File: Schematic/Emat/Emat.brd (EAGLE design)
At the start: 100 x 80 mm, 38 parts, among them J1 PIN1-2, J10 PIN1-2, J11 PIN1-2, J2 PIN1-2, J3 PIN1-2, J4 PIN1-2, J5 PIN1-2, J6 PIN1-2, J7 PIN1-2, J8 PIN1-2, J9 PIN1-2, Q2 STP13NM60NTO220BVH, U1 UCC27324D, X1 SMA-J502-ND

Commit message: Further work on schematic.
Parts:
- removed C8: 220p 630v, rcl:C1206K
- added C9: 220pF 1000V, rcl:C075-042X103
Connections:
- net N$13: now also C9.2; no longer C8.2
- net N$16: now also C9.1; no longer C8.1
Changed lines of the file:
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@@
 <element name="C6" library="rcl" package="C0805" value="1uF 16V" x="57.15" y="68.58" rot="R90"/>
 <element name="C7" library="rcl" package="C0805" value="1uF 16V" x="52.07" y="68.58" rot="R90"/>
-<element name="C8" library="rcl" package="C1206K" value="220p 630v" x="82.55" y="57.15" rot="R180"/>
 <element name="D1" library="diode" package="DO41-10" value="MUR160" x="88.9" y="43.18" rot="R180"/>
 <element name="D2" library="diode" package="DO41-10" value="MUR160" x="88.9" y="36.83" rot="R180"/>
@@
 <attribute name="OC_NEWARK" value="16H2318" x="-63.5" y="6.35" size="1.778" layer="27" display="off"/>
 </element>
+<element name="C9" library="rcl" package="C075-042X103" value="220pF 1000V" x="-63.5" y="-5.08"/>
 </elements>
 <signals>
@@
 </signal>
 <signal name="N$13">
-<contactref element="C8" pad="2"/>
 <contactref element="R10" pad="1"/>
-<wire x1="81.05" y1="57.15" x2="81.432" y2="53.34" width="0" layer="19" extent="1-1"/>
+<contactref element="C9" pad="2"/>
+<wire x1="-59.69" y1="-5.08" x2="81.432" y2="53.34" width="0" layer="19" extent="1-1"/>
 </signal>
 <signal name="N$14">
@@
 </signal>
 <signal name="N$16">
-<contactref element="C8" pad="1"/>
 <contactref element="C2" pad="2"/>
 <contactref element="C3" pad="2"/>
@@
 <contactref element="D2" pad="C"/>
 <contactref element="D1" pad="C"/>
-<wire x1="94.24" y1="55.88" x2="95.25" y2="68.58" width="0" layer="19" extent="1-1"/>
+<contactref element="C9" pad="1"/>
+<wire x1="95.25" y1="68.58" x2="95.25" y2="73.66" width="0" layer="19" extent="1-1"/>
+<wire x1="95.25" y1="62.23" x2="95.25" y2="68.58" width="0" layer="19" extent="1-1"/>
+<wire x1="94.24" y1="55.88" x2="95.25" y2="62.23" width="0" layer="19" extent="1-1"/>
 <wire x1="94.24" y1="49.53" x2="94.24" y2="55.88" width="0" layer="19" extent="1-1"/>
-<wire x1="95.25" y1="62.23" x2="94.24" y2="49.53" width="0" layer="19" extent="1-1"/>
-<wire x1="84.05" y1="57.15" x2="95.25" y2="62.23" width="0" layer="19" extent="1-1"/>
 <wire x1="93.98" y1="43.18" x2="94.24" y2="49.53" width="0" layer="19" extent="1-1"/>
 <wire x1="93.98" y1="36.83" x2="93.98" y2="43.18" width="0" layer="19" extent="1-1"/>
-<wire x1="95.25" y1="73.66" x2="93.98" y2="36.83" width="0" layer="19" extent="1-1"/>
+<wire x1="-67.31" y1="-5.08" x2="93.98" y2="36.83" width="0" layer="19" extent="1-1"/>
 </signal>
 <signal name="N$15">

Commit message: 300V PCB modified, BOM added.
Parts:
- C1, C2, C3: value 4.7n -> 4.7n 1000V
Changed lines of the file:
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@@
 </autorouter>
 <elements>
-<element name="C1" library="capacitor-wima" package="C10B4" value="4.7n" x="90.17" y="73.66"/>
-<element name="C2" library="capacitor-wima" package="C10B4" value="4.7n" x="90.17" y="68.58"/>
-<element name="C3" library="capacitor-wima" package="C10B4" value="4.7n" x="90.17" y="62.23"/>
+<element name="C1" library="capacitor-wima" package="C10B4" value="4.7n 1000V" x="90.17" y="73.66"/>
+<element name="C2" library="capacitor-wima" package="C10B4" value="4.7n 1000V" x="90.17" y="68.58"/>
+<element name="C3" library="capacitor-wima" package="C10B4" value="4.7n 1000V" x="90.17" y="62.23"/>
 <element name="C4" library="capacitor-wima" package="C27.5B13" value="1uF 400V" x="17.78" y="62.23" rot="R270"/>
 <element name="C5" library="rcl" package="SANYO-OSCON_G" value="47uF 400V" x="8.89" y="69.85"/>

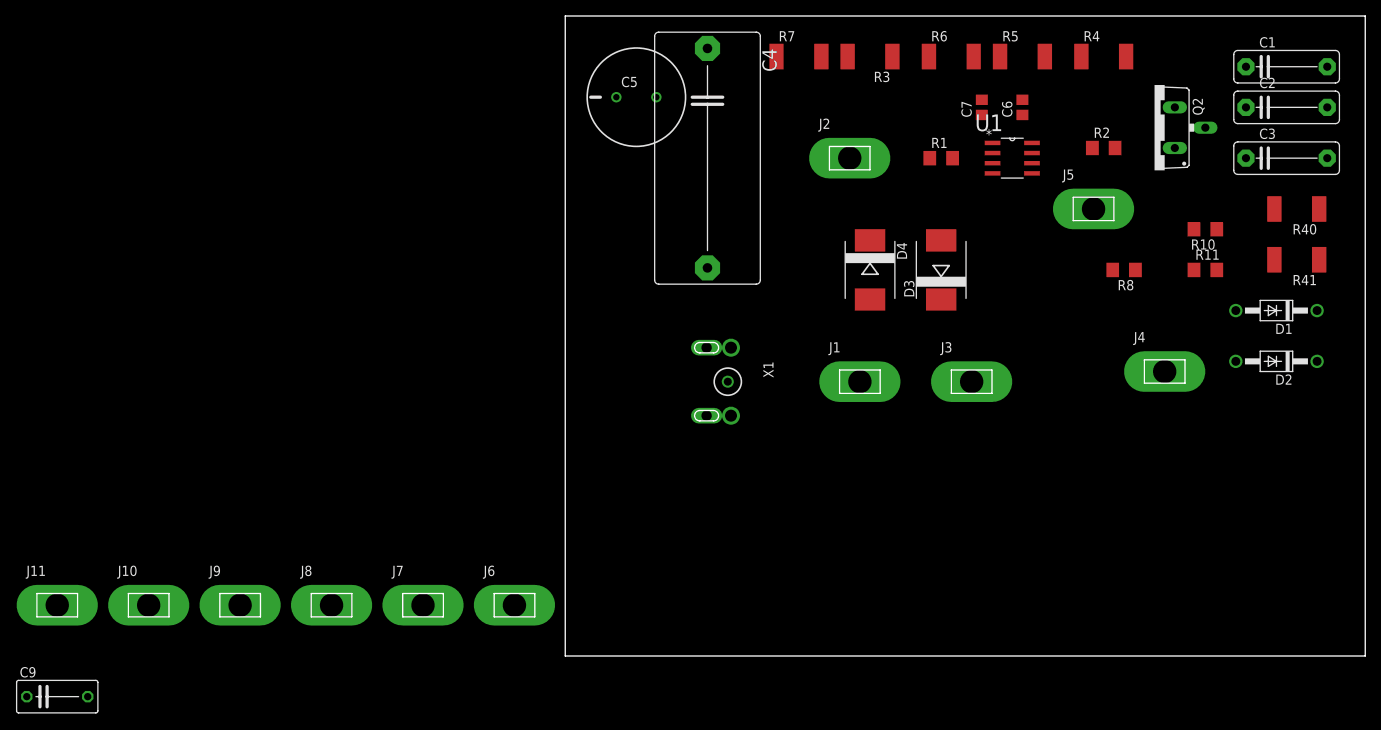
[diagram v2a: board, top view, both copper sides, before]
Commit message: Add switch tracing.
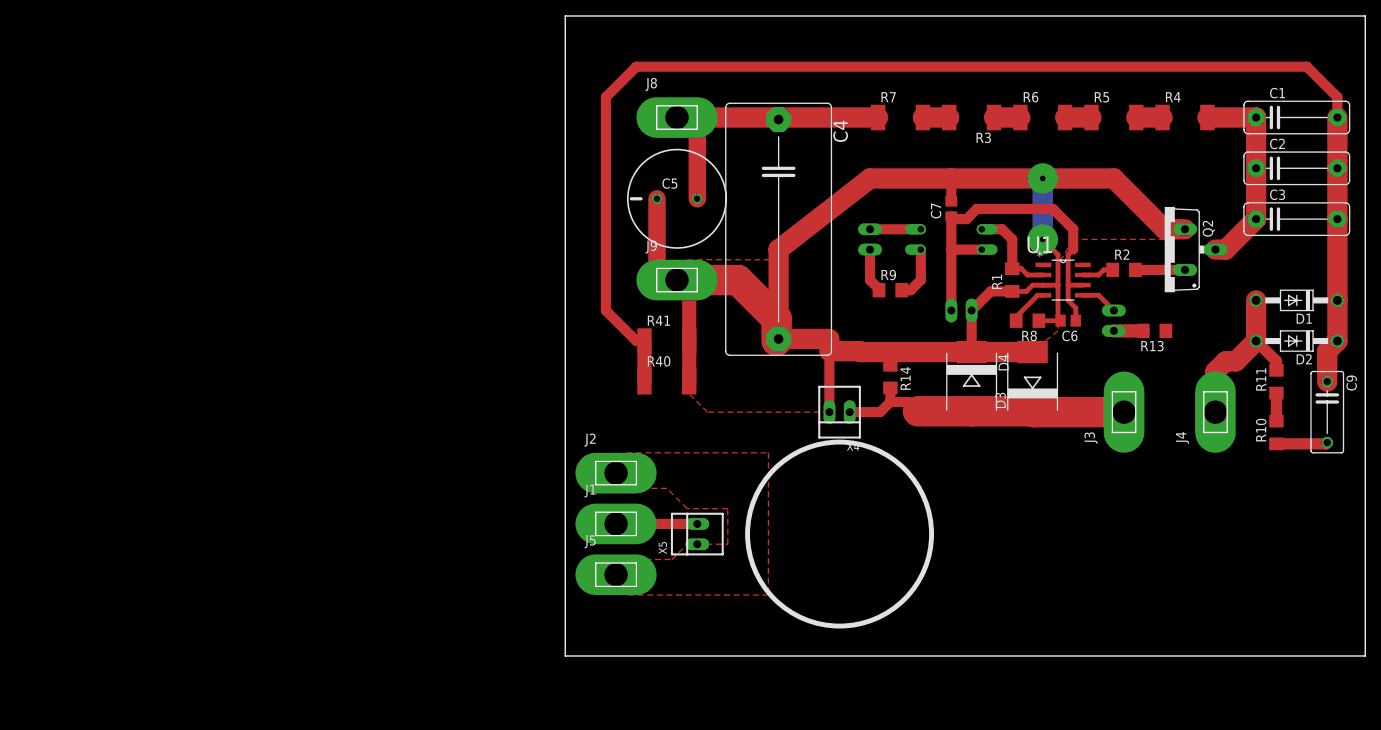
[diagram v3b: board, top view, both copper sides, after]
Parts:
- removed J10, J11, J6, J7: PIN1-2, con-faston:62221
- removed X1: SMA-J502-ND, con-coax:J502-ND
- added OK1: PC817, optocoupler:DIL04
- added R13: DNS, rcl:R1206
- added R14: 51, rcl:R1206
- added R9: 510, rcl:R1206
- added X2, X3, X4, X5, X6: 22-23-2021, con-molex:22-23-2021
- C6, C7: value 1uF 16V -> 1uF
- R1: value 51 -> 10K
- moved C9 162.7 mm to (95.2, 30.5), turned to 270 degrees
- moved R40 81.6 mm to (12.7, 34.3), turned to 0 degrees
- moved R41 79.4 mm to (12.7, 39.4), turned to 0 degrees
- moved J5 75.2 mm to (6.35, 10.2)
- moved J8 74.7 mm to (14.0, 67.3)
- moved J9 68.1 mm to (14.0, 47.0)
- moved J2 49.0 mm to (6.35, 22.9)
- moved J1 35.3 mm to (6.35, 16.5)
- moved C6 27.3 mm to (62.9, 41.9), turned to 180 degrees
- moved R10 26.9 mm to (88.9, 27.9), turned to 90 degrees
- moved J3 19.4 mm to (69.8, 30.5), turned to 90 degrees
- moved D4 18.9 mm to (50.8, 34.3)
- moved D3 18.1 mm to (58.4, 34.3)
- moved R1 17.6 mm to (55.9, 47.0), turned to 90 degrees
- moved R11 16.6 mm to (88.9, 34.3), turned to 90 degrees
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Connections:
- removed net N$5: J10.1, R1.1
- new net N$17: OK1.1, R9.2
- new net N$18: R9.1, X2.2
- new net N$19: OK1.2, X2.1
- new net N$20: D3.C, D4.A, J3.1, R14.2, X4.1
- new net N$21: R13.2, X6.2
- new net N$22: J2.1, J5.1, X5.1
- net +12V: now also OK1.4, X3.2; no longer J7.1
- net GND: now also R1.1, R14.1, X3.1, X4.2; no longer J11.1, J2.1, J6.1, X1.2, X1.3, X1.4, X1.5
- net N$1: now also OK1.3
- net N$10: now also X5.2; no longer D3.C, D4.A, J3.1, X1.1
- net N$12: now also X6.1; no longer J5.1
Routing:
- net GND: track 0.00 -> 196.2 mm, vias 0 -> 2
- net N$16: track 0.00 -> 168.8 mm
- net +12V: track 0.00 -> 46.4 mm
- net +UB: track 0.00 -> 38.1 mm
- net N$20: track 0.00 -> 37.1 mm
- net N$4: track 0.00 -> 25.4 mm
- net N$15: track 0.00 -> 21.5 mm
- net N$1: track 0.00 -> 12.2 mm
- net N$10: track 0.00 -> 10.2 mm
- net N$17: track 0.00 -> 6.72 mm
- net N$13: track 0.00 -> 6.41 mm
- net N$19: track 0.00 -> 6.35 mm
- net N$3: track 0.00 -> 6.20 mm
- net N$18: track 0.00 -> 5.54 mm
- net N$11: track 0.00 -> 5.00 mm
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- added copper zone on layer 1, net GND
- added copper zone on layer 1, net N$22
- added copper zone on layer 1, net N$5

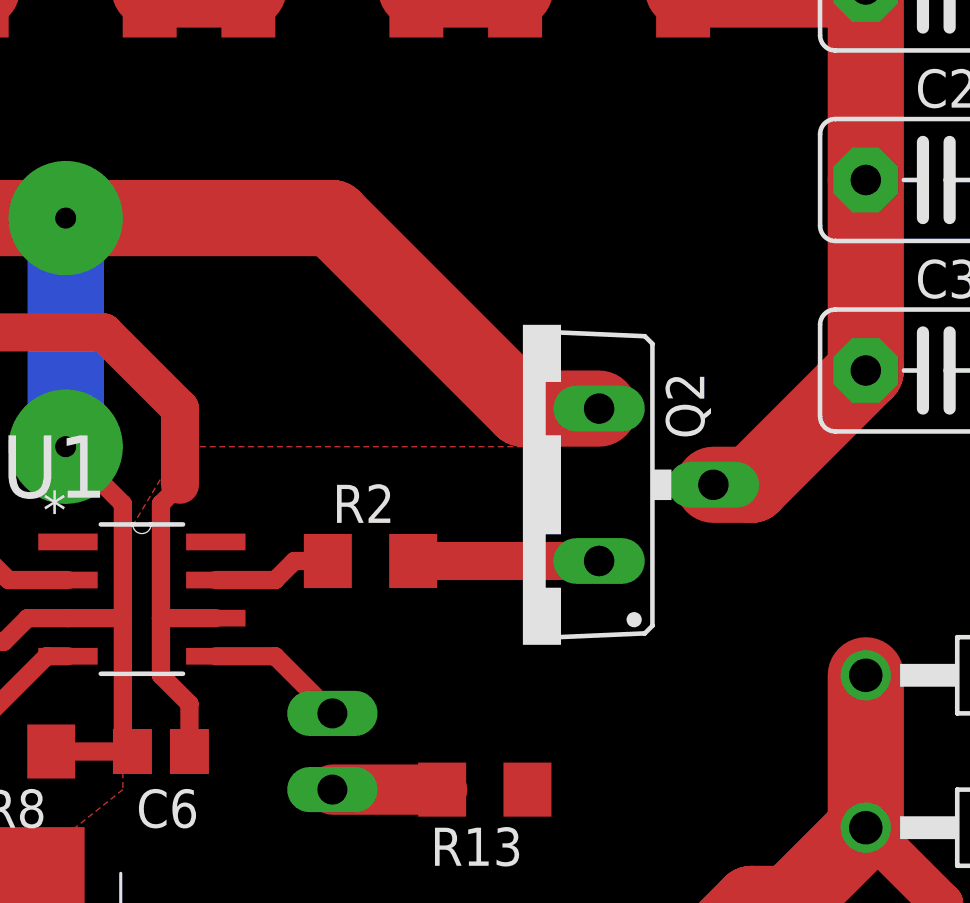
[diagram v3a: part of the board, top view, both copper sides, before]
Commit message: Modify board to fit to pcb.
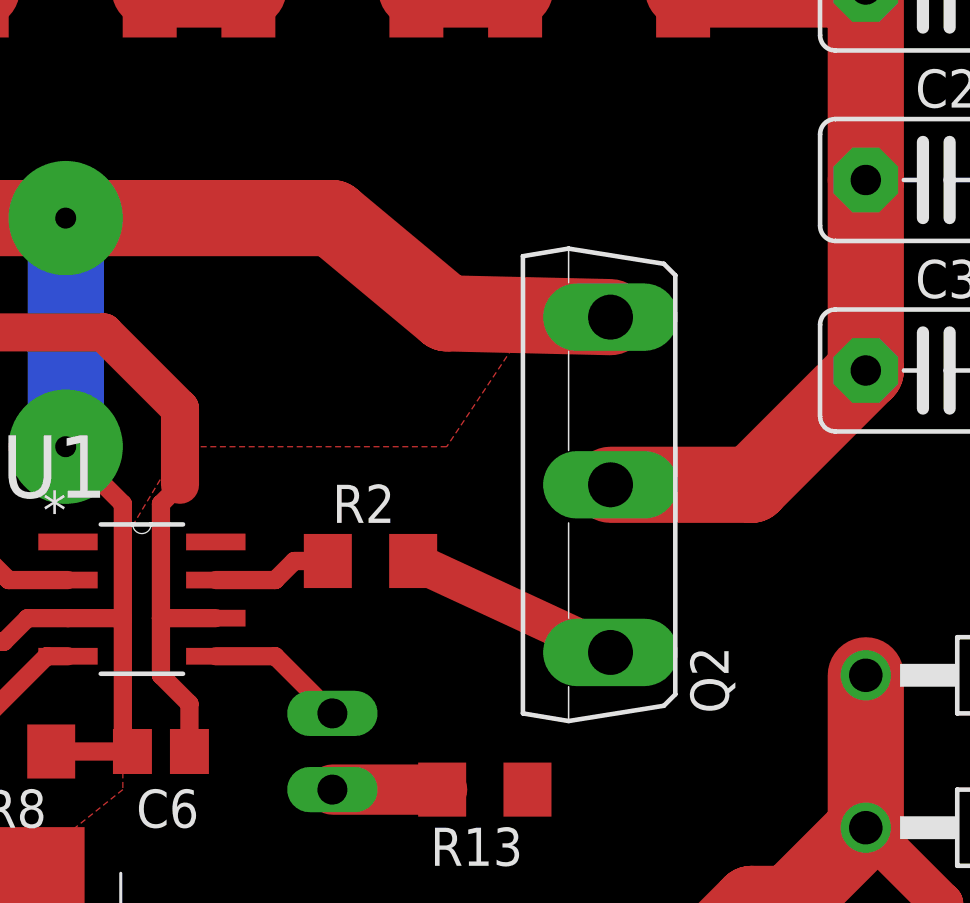
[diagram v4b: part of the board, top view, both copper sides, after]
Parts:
- Q2: value STP13NM60NTO220BVH -> STP13NM60NTO247BV; device transistor-power:TO220BVH -> transistor-power:TO247BV
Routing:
- net N$4: track 25.4 -> 28.9 mm
- net GND: track 196.2 -> 195.1 mm
- net N$3: track 6.20 -> 7.25 mm
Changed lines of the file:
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@@
 <attribute name="OC_NEWARK" value="16H2318" x="81.28" y="30.48" size="1.778" layer="27" rot="R90" display="off"/>
 </element>
-<element name="Q2" library="transistor-power" package="TO220BVH" value="STP13NM60NTO220BVH" x="74.93" y="50.8" rot="R90"/>
+<element name="Q2" library="transistor-power" package="TO247BV" value="STP13NM60NTO247BV" x="74.93" y="50.8" rot="R90"/>
 <element name="R1" library="rcl" package="R1206" value="10K" x="55.88" y="46.99" rot="R90"/>
 <element name="R10" library="rcl" package="R1206" value="510" x="88.9" y="27.94" rot="R90"/>
@@
 <contactref element="R2" pad="2"/>
 <contactref element="Q2" pad="G"/>
-<wire x1="71.272" y1="48.26" x2="77.47" y2="48.26" width="1.27" layer="1"/>
+<wire x1="71.272" y1="48.26" x2="77.851" y2="45.212" width="1.27" layer="1"/>
 </signal>
 <signal name="N$4">
@@
 <wire x1="86.36" y1="67.31" x2="86.36" y2="60.96" width="2.54" layer="1"/>
 <wire x1="86.36" y1="60.96" x2="86.36" y2="54.61" width="2.54" layer="1"/>
-<wire x1="81.28" y1="50.8" x2="82.55" y2="50.8" width="2.54" layer="1"/>
+<wire x1="77.851" y1="50.8" x2="82.55" y2="50.8" width="2.54" layer="1"/>
 <wire x1="82.55" y1="50.8" x2="86.36" y2="54.61" width="2.54" layer="1"/>
 </signal>
@@
 <wire x1="26.67" y1="50.8" x2="38.1" y2="59.69" width="2.54" layer="1"/>
 <wire x1="38.1" y1="59.69" x2="48.26" y2="59.69" width="2.54" layer="1"/>
-<wire x1="68.58" y1="59.69" x2="74.93" y2="53.34" width="2.54" layer="1"/>
-<wire x1="74.93" y1="53.34" x2="77.47" y2="53.34" width="2.54" layer="1"/>
+<wire x1="68.58" y1="59.69" x2="72.39" y2="56.515" width="2.54" layer="1"/>
+<wire x1="72.39" y1="56.515" x2="77.851" y2="56.388" width="2.54" layer="1"/>
 <wire x1="26.67" y1="39.624" x2="29.204" y2="39.63" width="2.54" layer="1"/>
 <wire x1="29.204" y1="39.63" x2="33.02" y2="39.63" width="2.54" layer="1"/>
@@
 <vertex x="38.1" y="59.69"/>
 <vertex x="67.31" y="59.69"/>
-<vertex x="74.93" y="53.34"/>
-<vertex x="74.93" y="52.07"/>
+<vertex x="74.93" y="55.88"/>
+<vertex x="72.39" y="52.07"/>
 <vertex x="63.5" y="52.07"/>
 <vertex x="61.595" y="48.895"/>
